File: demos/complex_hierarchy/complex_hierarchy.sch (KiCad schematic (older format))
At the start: 10 parts, among them P1 CONN_2, P2 CONN_2, U1 ICL7660, U2 78L05

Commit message: Update demos
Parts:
- C1, C10, C11, C2, C9: symbol CP -> complex_hierarchy_schlib:CP
- D1: symbol D_Small -> complex_hierarchy_schlib:D_Small
- P1, P2: symbol CONN_2 -> complex_hierarchy_schlib:CONN_2
- U1: symbol ICL7660 -> complex_hierarchy_schlib:ICL7660
- U2: symbol 7805 -> complex_hierarchy_schlib:7805
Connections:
- net +12C: now also U2.3 (VI); no longer U2.VI
- net GND: now also U2.2 (GND); no longer U2.GND
- net VCC: now also U2.1 (VO); no longer U2.VO
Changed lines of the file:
@@
-EESchema Schematic File Version 2
-LIBS:power
-LIBS:complex_hierarchy_schlib
+EESchema Schematic File Version 4
 LIBS:complex_hierarchy-cache
 EELAYER 26 0
@@
 	8800 2750 9350 2750
 $Comp
-L CP C10
+L complex_hierarchy_schlib:CP C10
 U 1 1 4B4B15E7
 P 6650 2750
@@
 $EndComp
 $Comp
-L GND #PWR01
+L complex_hierarchy_schlib:GND #PWR01
 U 1 1 4B4B15DA
 P 9050 2300
@@
 $EndComp
 $Comp
-L CP C11
+L complex_hierarchy_schlib:CP C11
 U 1 1 4B4B15D9
 P 9200 2500
@@
 NoConn ~ 7100 3050
 $Comp
-L -VAA #PWR02
+L complex_hierarchy_schlib:-VAA #PWR02
 U 1 1 4B4B1578
 P 9350 2750
@@
 $EndComp
 $Comp
-L 7805 U2
+L complex_hierarchy_schlib:7805 U2
 U 1 1 4B4B1532
 P 7900 1350
@@
 $EndComp
 $Comp
-L VCC #PWR03
+L complex_hierarchy_schlib:VCC #PWR03
 U 1 1 4B4B1253
 P 7900 2200
@@
 $EndComp
 $Comp
-L VCC #PWR04
+L complex_hierarchy_schlib:VCC #PWR04
 U 1 1 4B4B124E
 P 9200 1250
@@
 $EndComp
 $Comp
-L GND #PWR05
+L complex_hierarchy_schlib:GND #PWR05
 U 1 1 4B4B1237
 P 7900 3600
@@
 $EndComp
 $Comp
-L ICL7660 U1
+L complex_hierarchy_schlib:ICL7660 U1
 U 1 1 4B4B1230
 P 7950 2900
@@
 12Vext
 $Comp
-L CP C9
+L complex_hierarchy_schlib:CP C9
 U 1 1 4B3A1558
 P 2500 1500
@@
 $EndComp
 $Comp
-L GND #PWR06
+L complex_hierarchy_schlib:GND #PWR06
 U 1 1 4B3A1557
 P 2500 1700
@@
 $EndSheet
 $Comp
-L GND #PWR07
+L complex_hierarchy_schlib:GND #PWR07
 U 1 1 4B3A1302
 P 2200 1750
@@
 $EndComp
 $Comp
-L CONN_2 P1
+L complex_hierarchy_schlib:CONN_2 P1
 U 1 1 4B3A12F4
 P 1650 1400
@@
 $EndComp
 $Comp
-L HT #PWR08
+L complex_hierarchy_schlib:HT #PWR08
 U 1 1 4B0FA68B
 P 2500 1250
@@
 $EndComp
 $Comp
-L CP C1
+L complex_hierarchy_schlib:CP C1
 U 1 1 4B03CEC2
 P 9200 1600
@@
 $EndComp
 $Comp
-L GND #PWR09
+L complex_hierarchy_schlib:GND #PWR09
 U 1 1 4B03CEC1
 P 9200 1800
@@
 $EndComp
 $Comp
-L GND #PWR010
+L complex_hierarchy_schlib:GND #PWR010
 U 1 1 4B03CE88
 P 7900 1650
@@
 $EndComp
 $Comp
-L +12C #PWR011
+L complex_hierarchy_schlib:+12C #PWR011
 U 1 1 4B03CE6C
 P 7400 1250
@@
 $EndComp
 $Comp
-L PWR_FLAG #U012
+L complex_hierarchy_schlib:PWR_FLAG #U012
 U 1 1 4B03CAA3
 P 2200 1250
@@
 $EndComp
 $Comp
-L PWR_FLAG #U013
+L complex_hierarchy_schlib:PWR_FLAG #U013
 U 1 1 4B03C9F9
 P 3000 2450
@@
 $EndComp
 $Comp
-L +12C #PWR014
+L complex_hierarchy_schlib:+12C #PWR014
 U 1 1 4B03C68D
 P 3800 2450
@@
 $EndComp
 $Comp
-L PWR_FLAG #U015
+L complex_hierarchy_schlib:PWR_FLAG #U015
 U 1 1 4AE17C31
 P 2200 1650
@@
 $EndComp
 $Comp
-L +12V #U016
+L complex_hierarchy_schlib:+12V #U016
 U 1 1 4AE173EF
 P 3550 2450
@@
 $EndComp
 $Comp
-L GND #PWR017
+L complex_hierarchy_schlib:GND #PWR017
 U 1 1 4AE173D0
 P 3200 3000
@@
 $EndComp
 $Comp
-L CP C2
+L complex_hierarchy_schlib:CP C2
 U 1 1 4AE173CF
 P 3200 2750
@@
 $EndComp
 $Comp
-L D_Small D1
+L complex_hierarchy_schlib:D_Small D1
 U 1 1 4AE172F4
 P 2700 2500
@@
 $EndComp
 $Comp
-L GND #PWR018
+L complex_hierarchy_schlib:GND #PWR018
 U 1 1 4AD71B8E
 P 2100 2800
@@
 $EndComp
 $Comp
-L CONN_2 P2
+L complex_hierarchy_schlib:CONN_2 P2
 U 1 1 4AD71B06
 P 1650 2600

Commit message: Update demos
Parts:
- D1: footprint Discret:D5 -> Diode_THT:D_DO-41_SOD81_P12.70mm_Horizontal
- U1: footprint Housings_DIP:DIP-8_W7.62mm_LongPads -> Package_DIP:DIP-8_W7.62mm_LongPads
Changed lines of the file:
@@
 	8300 1300 9200 1300
 Wire Wire Line
-	2800 2500 3800 2500
-Wire Wire Line
-	2500 1250 2500 1350
+	2800 2500 3000 2500
+Wire Wire Line
+	2500 1250 2500 1300
 Wire Wire Line
 	3800 2500 3800 2450
@@
 	9200 1750 9200 1800
 Wire Wire Line
-	9200 1250 9200 1450
+	9200 1250 9200 1300
 Connection ~ 9200 1300
 Wire Wire Line
-	2200 1650 2200 1750
+	2200 1650 2200 1700
 Wire Wire Line
 	2500 1650 2500 1700
@@
 	7050 2650 7100 2650
 Wire Wire Line
-	8800 2750 9350 2750
+	8800 2750 9200 2750
 $Comp
 L complex_hierarchy_schlib:CP C10
@@
 F 0 "U1" H 7400 3300 70  0000 L CNN
 F 1 "ICL7660" H 8500 2450 70  0000 R CNN
-F 2 "Housings_DIP:DIP-8_W7.62mm_LongPads" H 8950 2300 60  0000 C CNN
+F 2 "Package_DIP:DIP-8_W7.62mm_LongPads" H 8950 2300 60  0000 C CNN
 F 3 "" H 7950 2900 60  0001 C CNN
 	1    7950 2900
@@
 F 0 "D1" H 2700 2400 40  0000 C CNN
 F 1 "1N4007" H 2700 2600 40  0000 C CNN
-F 2 "Discret:D5" H 2700 2350 30  0000 C CNN
+F 2 "Diode_THT:D_DO-41_SOD81_P12.70mm_Horizontal" H 2700 2350 30  0000 C CNN
 F 3 "" H 2700 2500 60  0001 C CNN
 	1    2700 2500
@@
 Connection ~ 2200 1300
 Wire Wire Line
-	2000 1300 2500 1300
+	2000 1300 2200 1300
 Wire Wire Line
 	2000 1500 2100 1500
@@
 Wire Wire Line
 	7900 3600 7900 3550
+Wire Wire Line
+	9200 2750 9350 2750
+Wire Wire Line
+	2500 1300 2500 1350
+Wire Wire Line
+	3200 2500 3550 2500
+Wire Wire Line
+	3550 2500 3800 2500
+Wire Wire Line
+	3000 2500 3200 2500
+Wire Wire Line
+	9200 1300 9200 1450
+Wire Wire Line
+	2200 1300 2500 1300
+Wire Wire Line
+	2200 1700 2200 1750
 $EndSCHEMATC

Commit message: Demos update
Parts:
- P1, P2: footprint Connect:bornier2 -> TerminalBlock_Phoenix:TerminalBlock_Phoenix_MKDS-1,5-2-5.08_1x02_P5.08mm_Horizontal
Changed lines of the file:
@@
 F 0 "P1" V 1600 1400 40  0000 C CNN
 F 1 "CONN_2" V 1700 1400 40  0000 C CNN
-F 2 "Connect:bornier2" H 1650 1200 30  0000 C CNN
+F 2 "TerminalBlock_Phoenix:TerminalBlock_Phoenix_MKDS-1,5-2-5.08_1x02_P5.08mm_Horizontal" H 1650 1200 30  0000 C CNN
 F 3 "" H 1650 1400 60  0001 C CNN
 	1    1650 1400
@@
 F 0 "P2" V 1600 2600 40  0000 C CNN
 F 1 "CONN_2" V 1700 2600 40  0000 C CNN
-F 2 "Connect:bornier2" H 1650 2400 30  0000 C CNN
+F 2 "TerminalBlock_Phoenix:TerminalBlock_Phoenix_MKDS-1,5-2-5.08_1x02_P5.08mm_Horizontal" H 1650 2400 30  0000 C CNN
 F 3 "" H 1650 2600 60  0001 C CNN
 	1    1650 2600

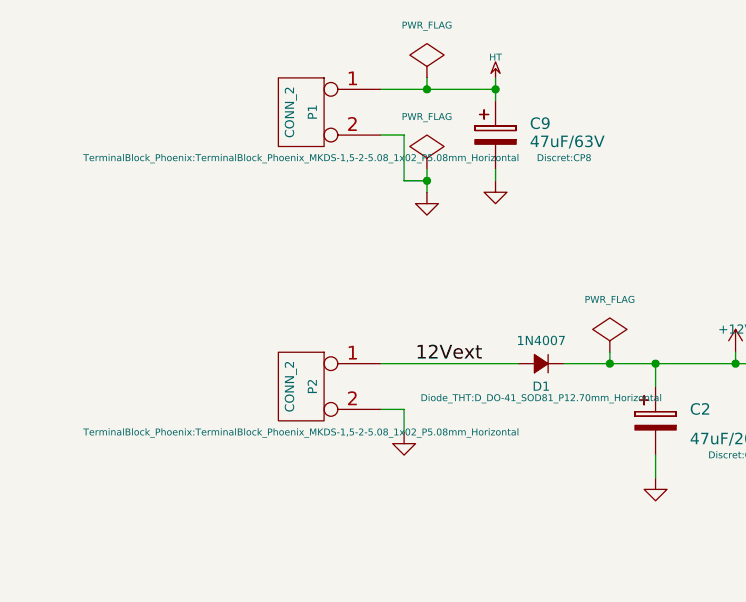
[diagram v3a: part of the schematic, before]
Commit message: Update demos to use recent footprints.
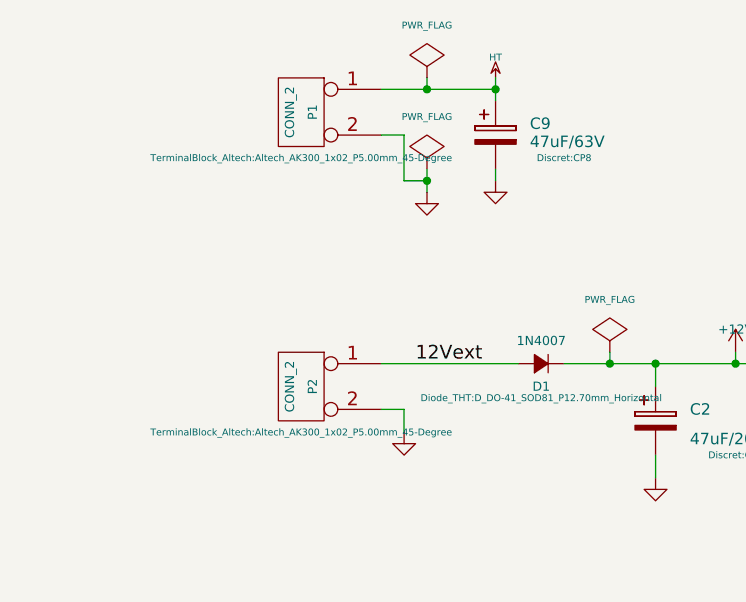
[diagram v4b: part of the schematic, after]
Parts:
- P1, P2: footprint TerminalBlock_Phoenix:TerminalBlock_Phoenix_MKDS-1,5-2-5.08_1x02_P5.08mm_Horizontal -> TerminalBlock_Altech:Altech_AK300_1x02_P5.00mm_45-Degree
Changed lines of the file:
@@
-EESchema Schematic File Version 4
+EESchema Schematic File Version 5
 LIBS:complex_hierarchy-cache
-EELAYER 26 0
+EELAYER 29 0
 EELAYER END
 $Descr A4 11693 8268
@@
 F 0 "P1" V 1600 1400 40  0000 C CNN
 F 1 "CONN_2" V 1700 1400 40  0000 C CNN
-F 2 "TerminalBlock_Phoenix:TerminalBlock_Phoenix_MKDS-1,5-2-5.08_1x02_P5.08mm_Horizontal" H 1650 1200 30  0000 C CNN
+F 2 "TerminalBlock_Altech:Altech_AK300_1x02_P5.00mm_45-Degree" H 1650 1200 30  0000 C CNN
 F 3 "" H 1650 1400 60  0001 C CNN
 	1    1650 1400
@@
 F 0 "P2" V 1600 2600 40  0000 C CNN
 F 1 "CONN_2" V 1700 2600 40  0000 C CNN
-F 2 "TerminalBlock_Phoenix:TerminalBlock_Phoenix_MKDS-1,5-2-5.08_1x02_P5.08mm_Horizontal" H 1650 2400 30  0000 C CNN
+F 2 "TerminalBlock_Altech:Altech_AK300_1x02_P5.00mm_45-Degree" H 1650 2400 30  0000 C CNN
 F 3 "" H 1650 2600 60  0001 C CNN
 	1    1650 2600

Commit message: Demos update
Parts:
- C1, C10, C11, C2: footprint Discret:CP6 -> Capacitor_THT:CP_Axial_L10.0mm_D4.5mm_P15.00mm_Horizontal
- C9: footprint Discret:CP8 -> Capacitor_THT:CP_Axial_L11.0mm_D6.0mm_P18.00mm_Horizontal
- U2: footprint Discret:LM78LXX -> Package_TO_SOT_THT:TO-92_HandSolder
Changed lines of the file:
@@
 EESchema Schematic File Version 5
-LIBS:complex_hierarchy-cache
-EELAYER 29 0
+EELAYER 30 0
 EELAYER END
 $Descr A4 11693 8268
@@
 Comment3 ""
 Comment4 ""
+Comment5 ""
+Comment6 ""
+Comment7 ""
+Comment8 ""
+Comment9 ""
 $EndDescr
 NoConn ~ 8800 3050
@@
 F 0 "C10" H 6800 2800 50  0000 L CNN
 F 1 "10uF" H 6800 2750 50  0000 L TNN
-F 2 "Discret:CP6" H 6850 2650 30  0000 C CNN
+F 2 "Capacitor_THT:CP_Axial_L10.0mm_D4.5mm_P15.00mm_Horizontal" H 6800 2650 10  0000 C CNN
 F 3 "" H 6650 2750 60  0001 C CNN
 	1    6650 2750
@@
 F 0 "#PWR01" H 9050 2300 30  0001 C CNN
 F 1 "GND" H 9050 2230 30  0001 C CNN
-F 2 "" H 9050 2300 60  0001 C CNN
+F 2 "" H 9050 2300 10  0001 C CNN
 F 3 "" H 9050 2300 60  0001 C CNN
 	1    9050 2300
@@
 F 0 "C11" H 9350 2550 50  0000 L CNN
 F 1 "10uF" H 9350 2500 50  0000 L TNN
-F 2 "Discret:CP6" H 9550 2400 30  0000 C CNN
+F 2 "Capacitor_THT:CP_Axial_L10.0mm_D4.5mm_P15.00mm_Horizontal" H 9550 2400 10  0000 C CNN
 F 3 "" H 9200 2500 60  0001 C CNN
 	1    9200 2500
@@
 F 0 "#PWR02" H 9350 2850 20  0001 C CNN
 F 1 "-VAA" V 9350 2950 40  0000 C CNN
-F 2 "" H 9350 2750 60  0001 C CNN
+F 2 "" H 9350 2750 10  0001 C CNN
 F 3 "" H 9350 2750 60  0001 C CNN
 	1    9350 2750
@@
 F 0 "U2" H 7900 1650 60  0000 C CNN
 F 1 "78L05" H 7900 1550 60  0000 C CNN
-F 2 "Discret:LM78LXX" H 8100 1150 30  0000 C CNN
+F 2 "Package_TO_SOT_THT:TO-92_HandSolder" H 8150 1150 10  0000 C CNN
 F 3 "" H 7900 1350 60  0001 C CNN
 	1    7900 1350
@@
 F 0 "#PWR03" H 7900 2300 30  0001 C CNN
 F 1 "VCC" H 7900 2300 40  0000 C CNN
-F 2 "" H 7900 2200 60  0001 C CNN
+F 2 "" H 7900 2200 10  0001 C CNN
 F 3 "" H 7900 2200 60  0001 C CNN
 	1    7900 2200
@@
 F 0 "#PWR04" H 9200 1350 30  0001 C CNN
 F 1 "VCC" H 9200 1350 40  0000 C CNN
-F 2 "" H 9200 1250 60  0001 C CNN
+F 2 "" H 9200 1250 10  0001 C CNN
 F 3 "" H 9200 1250 60  0001 C CNN
 	1    9200 1250
@@
 F 0 "#PWR05" H 7900 3600 30  0001 C CNN
 F 1 "GND" H 7900 3530 30  0001 C CNN
-F 2 "" H 7900 3600 60  0001 C CNN
+F 2 "" H 7900 3600 10  0001 C CNN
 F 3 "" H 7900 3600 60  0001 C CNN
 	1    7900 3600
@@
 F 0 "U1" H 7400 3300 70  0000 L CNN
 F 1 "ICL7660" H 8500 2450 70  0000 R CNN
-F 2 "Package_DIP:DIP-8_W7.62mm_LongPads" H 8950 2300 60  0000 C CNN
+F 2 "Package_DIP:DIP-8_W7.62mm_LongPads" H 8250 2350 10  0000 C CNN
 F 3 "" H 7950 2900 60  0001 C CNN
 	1    7950 2900
@@
 F 0 "C9" H 2650 1550 50  0000 L CNN
 F 1 "47uF/63V" H 2650 1500 50  0000 L TNN
-F 2 "Discret:CP8" H 2800 1400 30  0000 C CNN
+F 2 "Capacitor_THT:CP_Axial_L11.0mm_D6.0mm_P18.00mm_Horizontal" H 2800 1400 10  0000 C CNN
 F 3 "" H 2500 1500 60  0001 C CNN
 	1    2500 1500
@@
 F 0 "#PWR06" H 2500 1700 30  0001 C CNN
 F 1 "GND" H 2500 1630 30  0001 C CNN
-F 2 "" H 2500 1700 60  0001 C CNN
+F 2 "" H 2500 1700 10  0001 C CNN
 F 3 "" H 2500 1700 60  0001 C CNN
 	1    2500 1700
@@
 F 0 "#PWR07" H 2200 1750 30  0001 C CNN
 F 1 "GND" H 2200 1680 30  0001 C CNN
-F 2 "" H 2200 1750 60  0001 C CNN
+F 2 "" H 2200 1750 10  0001 C CNN
 F 3 "" H 2200 1750 60  0001 C CNN
 	1    2200 1750
@@
 F 0 "P1" V 1600 1400 40  0000 C CNN
 F 1 "CONN_2" V 1700 1400 40  0000 C CNN
-F 2 "TerminalBlock_Altech:Altech_AK300_1x02_P5.00mm_45-Degree" H 1650 1200 30  0000 C CNN
+F 2 "TerminalBlock_Altech:Altech_AK300_1x02_P5.00mm_45-Degree" H 1650 1200 10  0000 C CNN
 F 3 "" H 1650 1400 60  0001 C CNN
 	1    1650 1400
@@
 F 0 "#PWR08" H 2500 1370 20  0001 C CNN
 F 1 "HT" H 2500 1340 30  0000 C CNN
-F 2 "" H 2500 1250 60  0001 C CNN
+F 2 "" H 2500 1250 10  0001 C CNN
 F 3 "" H 2500 1250 60  0001 C CNN
 	1    2500 1250
@@
 F 0 "C1" H 9350 1650 50  0000 L CNN
 F 1 "47uF" H 9350 1600 50  0000 L TNN
-F 2 "Discret:CP6" H 9500 1500 30  0000 C CNN
+F 2 "Capacitor_THT:CP_Axial_L10.0mm_D4.5mm_P15.00mm_Horizontal" H 9500 1500 10  0000 C CNN
 F 3 "" H 9200 1600 60  0001 C CNN
 	1    9200 1600
@@
 F 0 "#PWR09" H 9200 1800 30  0001 C CNN
 F 1 "GND" H 9200 1730 30  0001 C CNN
-F 2 "" H 9200 1800 60  0001 C CNN
+F 2 "" H 9200 1800 10  0001 C CNN
 F 3 "" H 9200 1800 60  0001 C CNN
 	1    9200 1800
@@
 F 0 "#PWR010" H 7900 1650 30  0001 C CNN
 F 1 "GND" H 7900 1580 30  0001 C CNN
-F 2 "" H 7900 1650 60  0001 C CNN
+F 2 "" H 7900 1650 10  0001 C CNN
 F 3 "" H 7900 1650 60  0001 C CNN
 	1    7900 1650
@@
 F 0 "#PWR011" H 7400 1220 30  0001 C CNN
 F 1 "+12C" H 7400 1360 40  0000 C CNN
-F 2 "" H 7400 1250 60  0001 C CNN
+F 2 "" H 7400 1250 10  0001 C CNN
 F 3 "" H 7400 1250 60  0001 C CNN
 	1    7400 1250
@@
 F 0 "#U012" H 2200 1520 30  0001 C CNN
 F 1 "PWR_FLAG" H 2200 1480 30  0000 C CNN
-F 2 "" H 2200 1250 60  0001 C CNN
+F 2 "" H 2200 1250 10  0001 C CNN
 F 3 "" H 2200 1250 60  0001 C CNN
 	1    2200 1250
@@
 F 0 "#U013" H 3000 2720 30  0001 C CNN
 F 1 "PWR_FLAG" H 3000 2680 30  0000 C CNN
-F 2 "" H 3000 2450 60  0001 C CNN
+F 2 "" H 3000 2450 10  0001 C CNN
 F 3 "" H 3000 2450 60  0001 C CNN
 	1    3000 2450
@@
 F 0 "#PWR014" H 3800 2420 30  0001 C CNN
 F 1 "+12C" H 3800 2560 40  0000 C CNN
-F 2 "" H 3800 2450 60  0001 C CNN
+F 2 "" H 3800 2450 10  0001 C CNN
 F 3 "" H 3800 2450 60  0001 C CNN
 	1    3800 2450
@@
 F 0 "#U015" H 2200 1920 30  0001 C CNN
 F 1 "PWR_FLAG" H 2200 1880 30  0000 C CNN
-F 2 "" H 2200 1650 60  0001 C CNN
+F 2 "" H 2200 1650 10  0001 C CNN
 F 3 "" H 2200 1650 60  0001 C CNN
 	1    2200 1650
@@
 F 0 "#U016" H 3550 2400 20  0001 C CNN
 F 1 "+12V" H 3550 2550 40  0000 C CNN
-F 2 "" H 3550 2450 60  0001 C CNN
+F 2 "" H 3550 2450 10  0001 C CNN
 F 3 "" H 3550 2450 60  0001 C CNN
 	1    3550 2450
@@
 F 0 "#PWR017" H 3200 3000 30  0001 C CNN
 F 1 "GND" H 3200 2930 30  0001 C CNN
-F 2 "" H 3200 3000 60  0001 C CNN
+F 2 "" H 3200 3000 10  0001 C CNN
 F 3 "" H 3200 3000 60  0001 C CNN
 	1    3200 3000
@@
 F 0 "C2" H 3350 2800 50  0000 L CNN
 F 1 "47uF/20V" H 3350 2700 50  0000 L TNN
-F 2 "Discret:CP6" H 3550 2600 30  0000 C CNN
+F 2 "Capacitor_THT:CP_Axial_L10.0mm_D4.5mm_P15.00mm_Horizontal" H 3550 2600 10  0000 C CNN
 F 3 "" H 3200 2750 60  0001 C CNN
 	1    3200 2750
@@
 F 0 "D1" H 2700 2400 40  0000 C CNN
 F 1 "1N4007" H 2700 2600 40  0000 C CNN
-F 2 "Diode_THT:D_DO-41_SOD81_P12.70mm_Horizontal" H 2700 2350 30  0000 C CNN
+F 2 "Diode_THT:D_DO-41_SOD81_P12.70mm_Horizontal" H 2700 2350 10  0000 C CNN
 F 3 "" H 2700 2500 60  0001 C CNN
 	1    2700 2500
@@
 F 0 "#PWR018" H 2100 2800 30  0001 C CNN
 F 1 "GND" H 2100 2730 30  0001 C CNN
-F 2 "" H 2100 2800 60  0001 C CNN
+F 2 "" H 2100 2800 10  0001 C CNN
 F 3 "" H 2100 2800 60  0001 C CNN
 	1    2100 2800
@@
 F 0 "P2" V 1600 2600 40  0000 C CNN
 F 1 "CONN_2" V 1700 2600 40  0000 C CNN
-F 2 "TerminalBlock_Altech:Altech_AK300_1x02_P5.00mm_45-Degree" H 1650 2400 30  0000 C CNN
+F 2 "TerminalBlock_Altech:Altech_AK300_1x02_P5.00mm_45-Degree" H 1650 2400 10  0000 C CNN
 F 3 "" H 1650 2600 60  0001 C CNN
 	1    1650 2600
